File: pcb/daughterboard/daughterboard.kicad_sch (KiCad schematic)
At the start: 2 parts, among them J1 Conn_01x20_Pin, J22 Conn_01x20_Pin

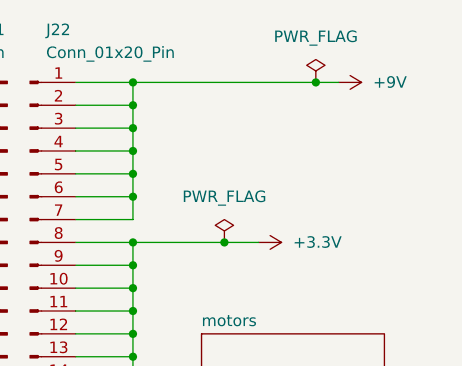
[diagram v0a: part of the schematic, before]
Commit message: changing powerline
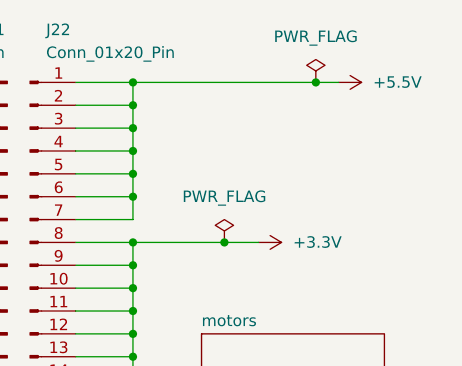
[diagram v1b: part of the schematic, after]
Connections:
- net +9V renamed +5.5V
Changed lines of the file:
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@@
 			)
 		)
-		(property "Value" "+9V"
+		(property "Value" "+5.5V"
 			(at 191.77 66.0399 90)
 			(show_name no)

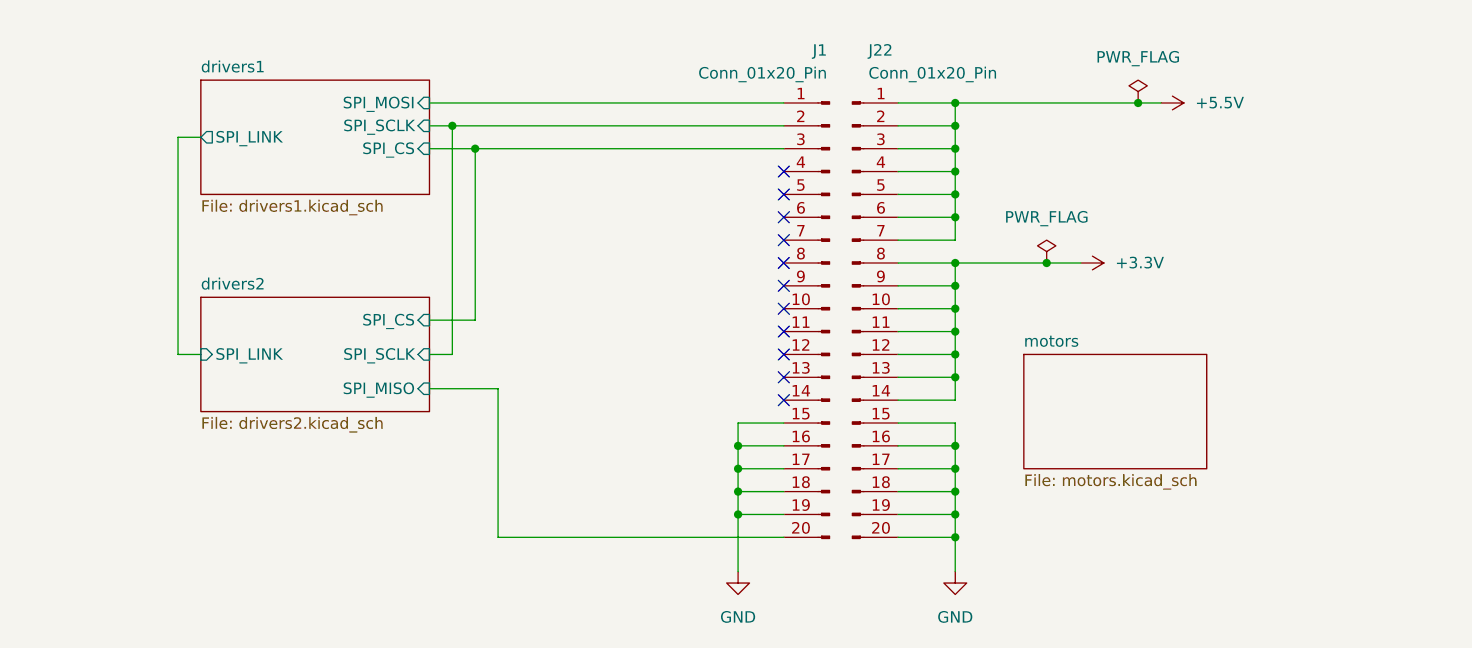
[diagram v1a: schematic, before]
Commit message: addec electrolytic capacitors on 5v5 line
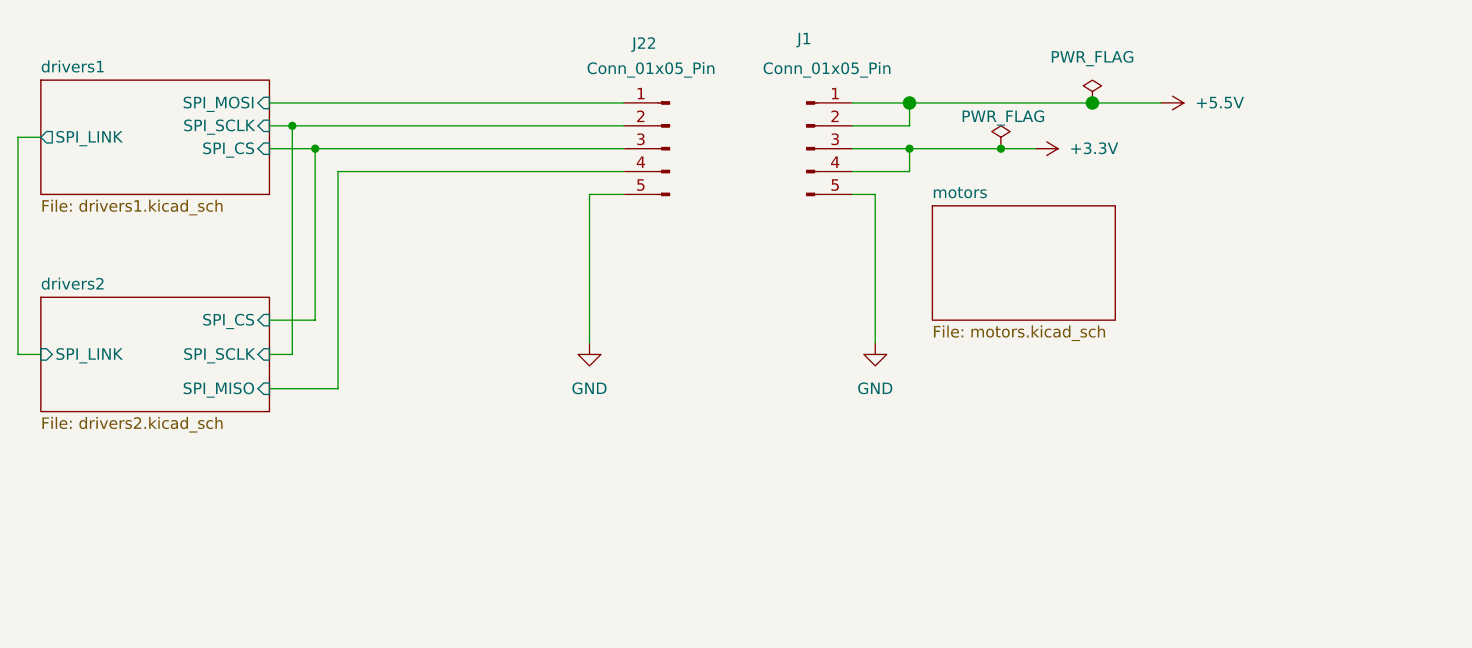
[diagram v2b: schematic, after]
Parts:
- removed J1, J22: Conn_01x20_Pin, Connector_PinHeader_2.54mm:PinHeader_1x20_P2.54mm_Horizontal, symbol Connector:Conn_01x20_Pin
- added J1, J22: Conn_01x05_Pin, symbol Connector:Conn_01x05_Pin
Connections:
- net +3.3V: now also J1.3 (Pin_3), J1.4 (Pin_4)
- net +5.5V: now also J1.1 (Pin_1), J1.2 (Pin_2)
- net GND: now also J1.5 (Pin_5), J22.5 (Pin_5)
- net drivers1/SPI_CS: now also J22.3 (Pin_3)
- net drivers1/SPI_MOSI: now also J22.1 (Pin_1)
- net drivers1/SPI_SCLK: now also J22.2 (Pin_2)
- net drivers2/SPI_MISO: now also J22.4 (Pin_4)
- no-connect marks 11 -> 0

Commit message: added initial power lines
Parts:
- removed J1, J22: Conn_01x05_Pin, symbol Connector:Conn_01x05_Pin
- added J1, J2: M20-9960646, A_HANU_FOOTPRINTS:HDRRA6W64P0X254_1X6_1524X254X254P, symbol M20-9960646:M20-9960646
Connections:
- net +3.3V: now also J2.3, J2.4
- net +5.5V: now also J2.1, J2.2
- net GND: now also J1.5, J2.5
- net drivers1/SPI_CS: now also J1.3
- net drivers1/SPI_MOSI: now also J1.1
- net drivers1/SPI_SCLK: now also J1.2
- net drivers2/SPI_MISO: now also J1.4
- no-connect marks 0 -> 2

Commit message: added routes for some motor-connectors
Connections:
- net GND: now also J1.6, J2.6
- no-connect marks 2 -> 0
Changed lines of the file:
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@@
+	)
+	(junction
+		(at 177.8 78.74)
+		(diameter 0)
+		(color 0 0 0 1)
+	)
+	(junction
+		(at 124.46 78.74)
+		(diameter 0)
+		(color 0 0 0 1)
 	)
 	(junction
@@
 		(color 255 0 0 1)
 	)
-	(no_connect
-		(at 175.26 78.74)
-	)
-	(no_connect
-		(at 128.27 78.74)
-	)
 	(wire
 		(pts
@@
 	(wire
 		(pts
-			(xy 124.46 76.2) (xy 124.46 92.71)
+			(xy 177.8 78.74) (xy 177.8 92.71)
+		)
+		(stroke
+			(width 0)
+			(type default)
+			(color 0 0 0 1)
+		)
+	)
+	(wire
+		(pts
+			(xy 124.46 76.2) (xy 124.46 78.74)
 		)
 		(stroke
@@
 	(wire
 		(pts
-			(xy 177.8 76.2) (xy 177.8 92.71)
+			(xy 177.8 76.2) (xy 177.8 78.74)
 		)
 		(stroke
@@
 	(wire
 		(pts
+			(xy 175.26 78.74) (xy 177.8 78.74)
+		)
+		(stroke
+			(width 0)
+			(type default)
+			(color 0 0 0 1)
+		)
+	)
+	(wire
+		(pts
 			(xy 88.9 68.58) (xy 91.44 68.58)
 		)
@@
 	(wire
 		(pts
+			(xy 124.46 78.74) (xy 128.27 78.74)
+		)
+		(stroke
+			(width 0)
+			(type default)
+			(color 0 0 0 1)
+		)
+	)
+	(wire
+		(pts
 			(xy 181.61 73.66) (xy 181.61 71.12)
 		)
@@
 		)
 	)
+	(wire
+		(pts
+			(xy 124.46 78.74) (xy 124.46 92.71)
+		)
+		(stroke
+			(width 0)
+			(type default)
+			(color 0 0 0 1)
+		)
+	)

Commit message: fixed missing libraries for daughterboard
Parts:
- J1, J2: footprint A_HANU_FOOTPRINTS:HDRRA6W64P0X254_1X6_1524X254X254P -> KiCad7:HDRRA6W64P0X254_1X6_1524X254X254P
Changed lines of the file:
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@@
 			)
 		)
-		(property "Footprint" "A_HANU_FOOTPRINTS:HDRRA6W64P0X254_1X6_1524X254X254P"
+		(property "Footprint" "KiCad7:HDRRA6W64P0X254_1X6_1524X254X254P"
 			(at 158.75 160.96 0)
 			(hide yes)
@@
 			)
 		)
-		(property "Footprint" "A_HANU_FOOTPRINTS:HDRRA6W64P0X254_1X6_1524X254X254P"
+		(property "Footprint" "KiCad7:HDRRA6W64P0X254_1X6_1524X254X254P"
 			(at 144.78 160.96 0)
 			(hide yes)

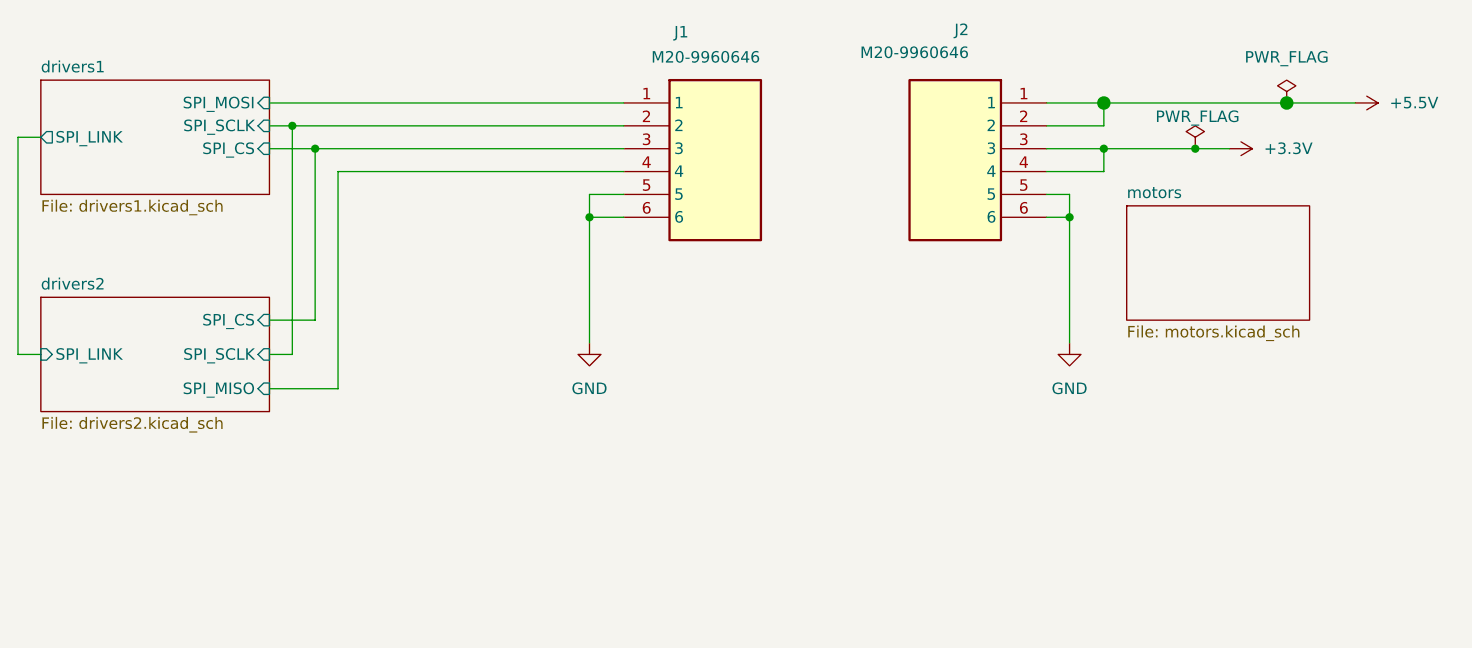
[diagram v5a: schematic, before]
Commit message: Initial pcb design for daughterboard Added 3D models for components Modified the daughterboard to motherboard connectors Removed 220uF capacitors from the 5V5 power line
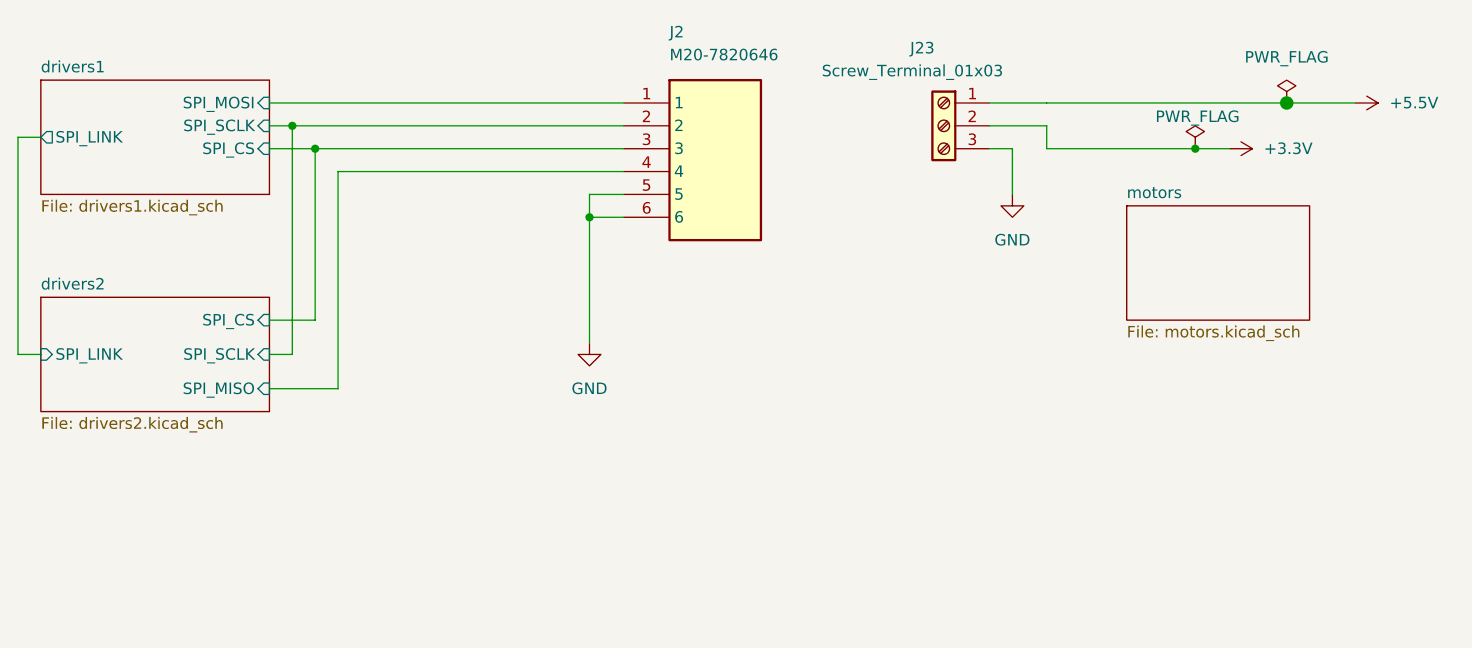
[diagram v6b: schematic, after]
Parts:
- removed J1, J2: M20-9960646, KiCad7:HDRRA6W64P0X254_1X6_1524X254X254P, symbol M20-9960646:M20-9960646
- added J2: M20-7820646, M20-7820646:HDRV6W70P0X254_1X6_1564X250X850P, symbol KiCad4:M20-7820646
- added J23: Screw_Terminal_01x03, TerminalBlock_Phoenix:TerminalBlock_Phoenix_MKDS-1,5-3-5.08_1x03_P5.08mm_Horizontal, symbol Connector:Screw_Terminal_01x03
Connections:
- net +3.3V: now also J23.2 (Pin_2)
- net +5.5V: now also J23.1 (Pin_1)
- net GND: now also J2.5, J2.6, J23.3 (Pin_3)
- net drivers1/SPI_CS: now also J2.3
- net drivers1/SPI_MOSI: now also J2.1
- net drivers1/SPI_SCLK: now also J2.2
- net drivers2/SPI_MISO: now also J2.4

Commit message: Finalized daughterboard pcb design 0 errors Verified every 3D model, footprint According to the schematic
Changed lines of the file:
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@@
 			)
 		)
-		(pin "SPI_MISO" input
+		(pin "SPI_MISO" output
 			(at 88.9 97.79 0)
 			(effects

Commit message: Final touches for the PCB order Added MPN, Description, checked footprints and 3D models Finished the BOM
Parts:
- J23: Manufacturer_Name (none) -> Harwin; Manufacturer_Part_Number (none) -> M20-7820646
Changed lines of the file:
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@@
+			)
+		)
+		(property "Manufacturer_Name" "Harwin"
+			(at 163.83 68.58 0)
+			(hide yes)
+			(show_name no)
+			(do_not_autoplace no)
+			(effects
+				(font
+					(size 1.27 1.27)
+				)
+			)
+		)
+		(property "Manufacturer_Part_Number" "M20-7820646"
+			(at 163.83 68.58 0)
+			(hide yes)
+			(show_name no)
+			(do_not_autoplace no)
+			(effects
+				(font
+					(size 1.27 1.27)
+				)
 			)
 		)
